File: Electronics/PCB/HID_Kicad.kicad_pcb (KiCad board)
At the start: 2 copper layers, 78.7 x 55.9 mm, 11 parts, among them J1_encoder1 Conn_01x05_Male, J2_Switches1 Conn_01x05_Male

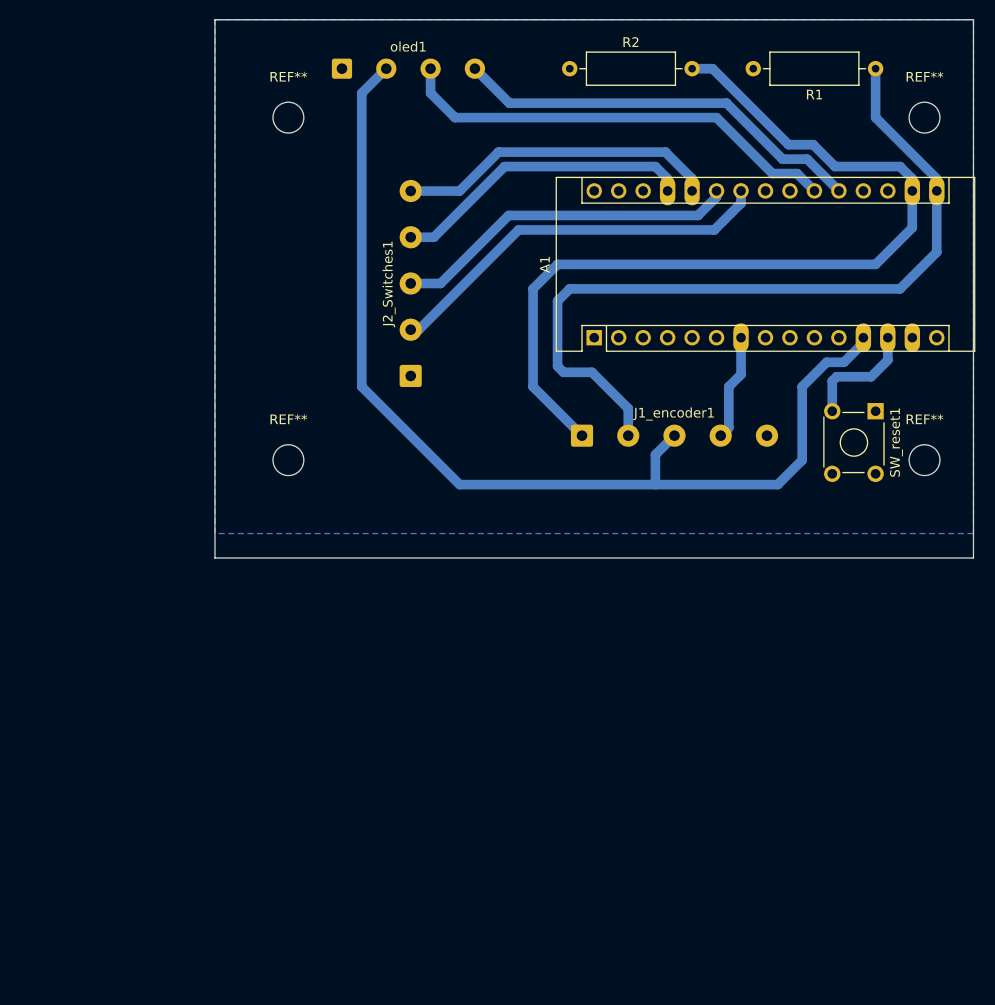
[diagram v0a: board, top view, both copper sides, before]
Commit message: updated pcb layout, added vcc for switches
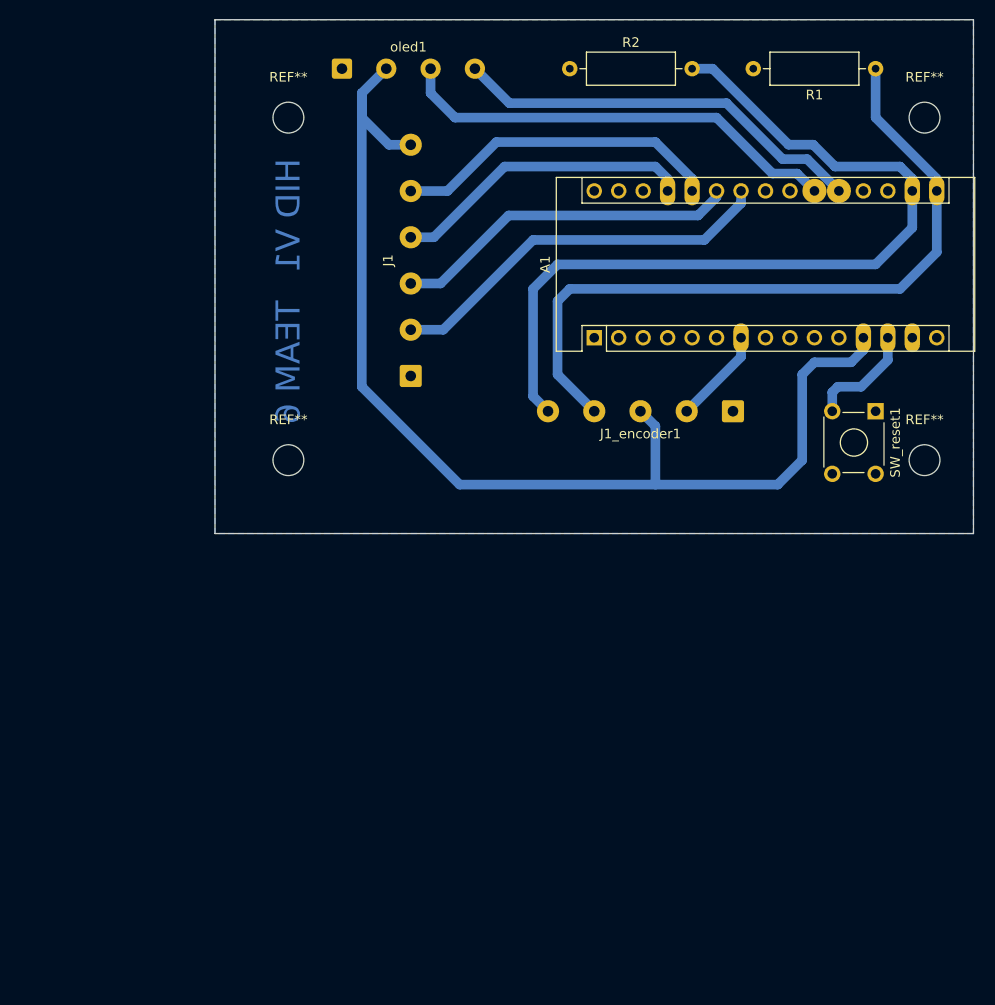
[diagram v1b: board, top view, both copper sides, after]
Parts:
- removed J2_Switches1: Conn_01x05_Male, Connector_Wire:SolderWire-0.5sqmm_1x05_P4.8mm_D0.9mm_OD2.3mm
- added J1: Conn_01x06_Male, Connector_Wire:SolderWire-0.5sqmm_1x06_P4.8mm_D0.9mm_OD2.3mm, F.Cu at (129.5, 59.8)
- moved J1_encoder1 15.9 mm to (163.0, 63.5), turned to 180 degrees
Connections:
- A1 pad 7: Net-(J1_encoder1-Pad4) -> Net-(A1-Pad7)
- J1_encoder1 pad 1: Net-(A1-Pad17) -> GND
- J1_encoder1 pad 2: Net-(A1-Pad16) -> Net-(A1-Pad7)
- J1_encoder1 pad 4: Net-(J1_encoder1-Pad4) -> Net-(A1-Pad16)
- J1_encoder1 pad 5: GND -> Net-(A1-Pad17)
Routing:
- net VCC: track 107.3 -> 119.7 mm
- net Net-(J1_encoder1-Pad4): track 11.0 -> 0.00 mm
- net Net-(A1-Pad7): track 0.00 -> 9.97 mm
- net Net-(A1-Pad16): track 81.9 -> 76.2 mm
- net Net-(A1-Pad17): track 92.0 -> 88.0 mm
- net Net-(A1-Pad26): track 33.3 -> 34.2 mm
- net Net-(A1-Pad13): track 12.1 -> 11.4 mm
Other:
- board size 78.7 x 55.9 mm -> 78.7 x 53.3 mm
- board text added: "HID V1"
- board text added: "TEAM 6"

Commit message: PCB design updated to fit inside enclosure
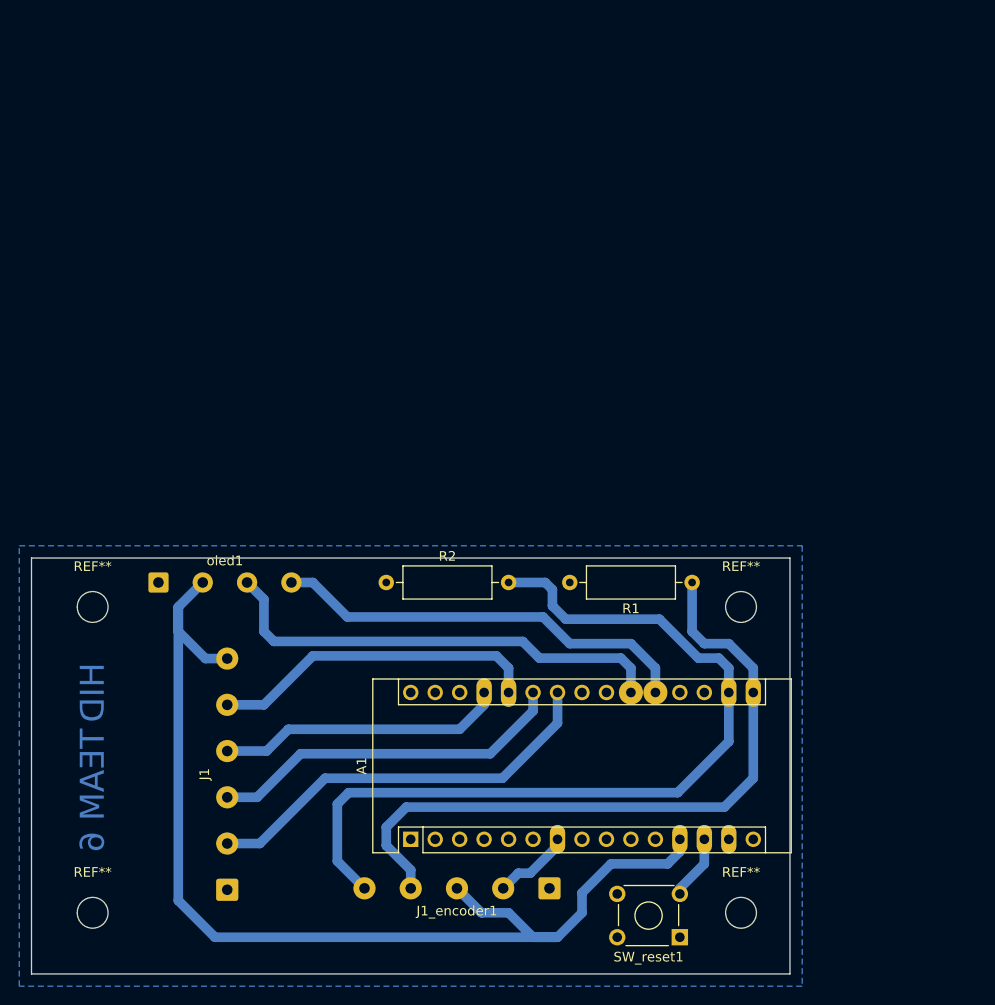
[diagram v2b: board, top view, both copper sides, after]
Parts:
- moved SW_reset1 58.3 mm to (157.5, 118.1), turned to 180 degrees
- moved J1 56.6 mm to (110.5, 113.2)
- moved R1 56.6 mm to (158.8, 81.3)
- moved R2 56.6 mm to (127.0, 81.3)
- moved oled1 56.6 mm to (103.3, 81.3)
- moved A1 55.4 mm to (129.5, 107.9)
- moved REF** 54.7 mm to (96.5, 83.8)
- moved REF** 54.3 mm to (163.8, 83.8)
- moved J1_encoder1 53.1 mm to (143.9, 113.0)
- moved REF** 51.2 mm to (96.5, 115.6)
- moved REF** 50.7 mm to (163.8, 115.6)
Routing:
- net Net-(A1-Pad13): track 11.4 -> 6.72 mm
- net VCC: track 119.7 -> 115.2 mm
- net Net-(A1-Pad16): track 76.2 -> 72.0 mm
- net Net-(A1-Pad7): track 9.97 -> 8.15 mm
- net Net-(A1-Pad24): track 41.0 -> 42.7 mm
- net Net-(A1-Pad27): track 31.5 -> 29.9 mm
- net Net-(oled1-Pad3): track 46.6 -> 48.0 mm
- net Net-(A1-Pad25): track 36.1 -> 37.4 mm
- net Net-(A1-Pad20): track 43.0 -> 44.0 mm
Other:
- board size 78.7 x 53.3 mm -> 78.7 x 43.2 mm
- board text added: "HID"
- board text removed: "HID V1"
